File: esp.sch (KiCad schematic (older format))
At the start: 11 parts, among them J1 JTAG, U1 ESP32-WROOM-32

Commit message: Added images Added information to schematic Added information to layout
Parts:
- renumbered C5 to C4, C6 to C5
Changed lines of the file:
@@
 encoding utf-8
 Sheet 2 11
-Title ""
-Date ""
-Rev ""
-Comp ""
-Comment1 ""
+Title "AirMon"
+Date "2020-01-13"
+Rev "0.1"
+Comp "Jörg Bayer"
+Comment1 "CC BY 4.0"
 Comment2 ""
 Comment3 ""
@@
 U 1 1 5E199A3D
 P 4950 2900
-F 0 "D1" H 4942 2645 50  0000 C CNN
-F 1 "GREEN" H 4942 2736 50  0000 C CNN
+F 0 "D1" H 4900 3000 50  0000 C CNN
+F 1 "GREEN" H 5100 3000 50  0000 C CNN
 F 2 "Diode_SMD:D_0805_2012Metric" H 4950 2900 50  0001 C CNN
 F 3 "~" H 4950 2900 50  0001 C CNN
@@
 AR Path="/5DD6D4DA/5DDED074/5DEEC855" Ref="C?"  Part="1"
 AR Path="/5E15DEC3/5DEEC855" Ref="C?"  Part="1"
-AR Path="/5E151517/5DEEC855" Ref="C5"  Part="1"
-F 0 "C5" H 4915 4596 50  0000 L CNN
+AR Path="/5E151517/5DEEC855" Ref="C4"  Part="1"
+F 0 "C4" H 4915 4596 50  0000 L CNN
 F 1 "100n" H 4915 4505 50  0000 L CNN
 F 2 "Capacitor_SMD:C_0603_1608Metric" H 4838 4400 50  0001 C CNN
@@
 AR Path="/5DD6D4DA/5DDED074/5E1DF3B6" Ref="C?"  Part="1"
 AR Path="/5E15DEC3/5E1DF3B6" Ref="C?"  Part="1"
-AR Path="/5E151517/5E1DF3B6" Ref="C6"  Part="1"
-F 0 "C6" H 5715 2996 50  0000 L CNN
+AR Path="/5E151517/5E1DF3B6" Ref="C5"  Part="1"
+F 0 "C5" H 5715 2996 50  0000 L CNN
 F 1 "100n" H 5715 2905 50  0000 L CNN
 F 2 "Capacitor_SMD:C_0603_1608Metric" H 5638 2800 50  0001 C CNN

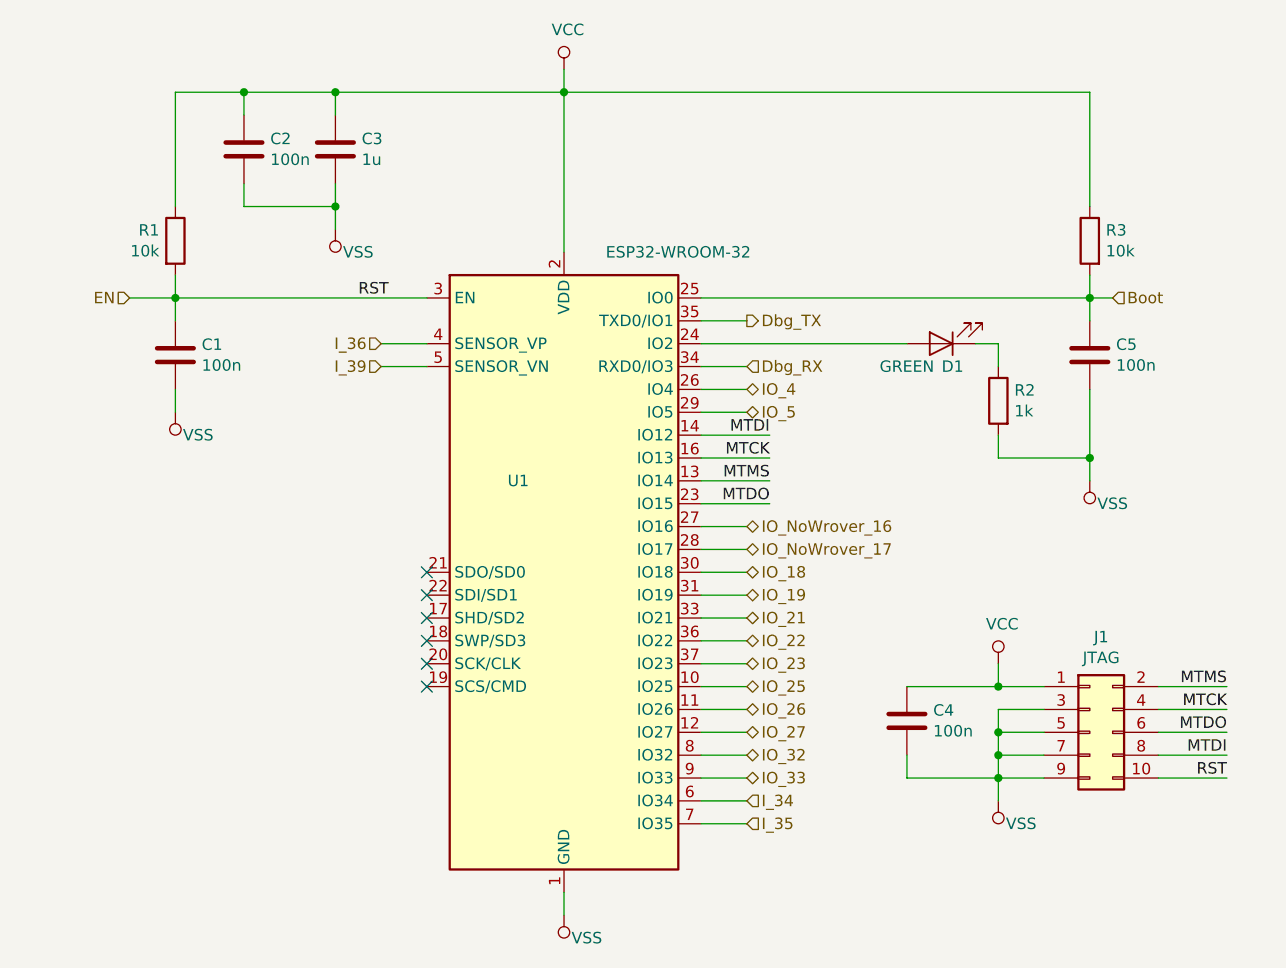
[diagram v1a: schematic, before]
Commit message: Added fuse for USB Added buttons for boot and reset Added version number to PCB Changed several component values for improved manufacturing Added BOM Added component position file
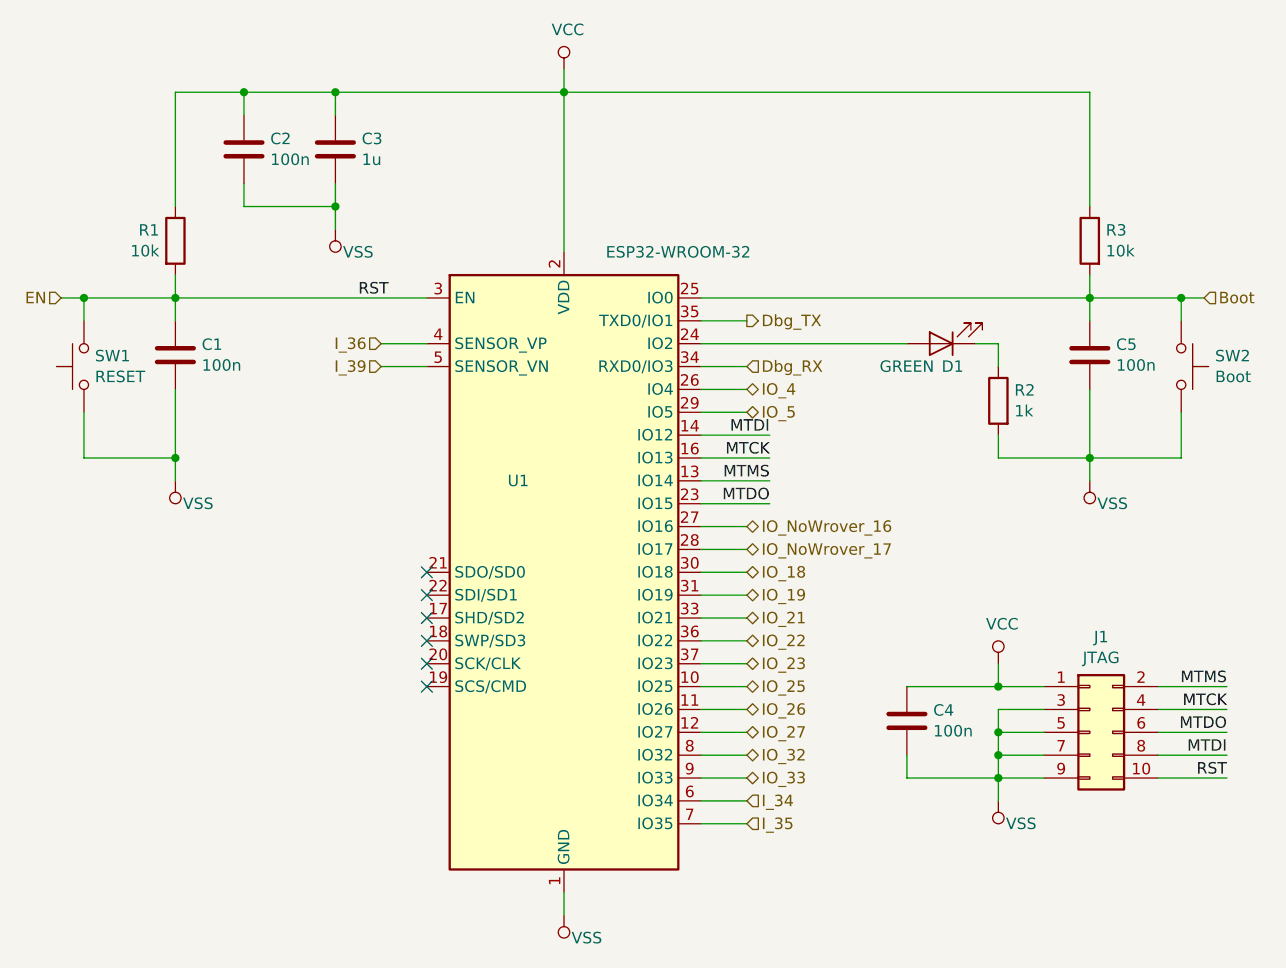
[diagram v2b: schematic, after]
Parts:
- added SW1: RESET, Button_Switch_SMD:SW_SPST_SKQG_WithStem, symbol Switch:SW_Push
- added SW2: Boot, Button_Switch_SMD:SW_SPST_SKQG_WithStem, symbol Switch:SW_Push
- C1, C2, C4, C5: lcsc# (none) -> C14663; manf# CL10B104KB8NNNL -> CC0603KRX7R9BB104
- C3: lcsc# (none) -> C28323; manf# CL21B105KBFNNNG -> CL21B105KBFNNNE
- D1: lcsc# (none) -> C2297
- J1: lcsc# (none) -> C180221; manf# (none) -> 20021221-00010C4LF
- R1, R3: lcsc# (none) -> C25804; manf# (none) -> 0603WAF1002T5E
- R2: lcsc# (none) -> C17513; manf# (none) -> 0805W8F1001T5E
- U1: manf# (none) -> ESP32-WROOM-32
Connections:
- net Boot: now also SW2.1
- net EN: now also SW1.1
- net VSS: now also SW1.2, SW2.2
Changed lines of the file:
@@
 F 2 "RF_Module:ESP32-WROOM-32" H 3300 2400 50  0001 C CNN
 F 3 "https://www.espressif.com/sites/default/files/documentation/esp32-wroom-32_datasheet_en.pdf" H 3000 3950 50  0001 C CNN
+F 4 "ESP32-WROOM-32" H 0   0   50  0001 C CNN "manf#"
 	1    3300 3900
 	1    0    0    -1
@@
 F 2 "Diode_SMD:D_0805_2012Metric" H 4950 2900 50  0001 C CNN
 F 3 "~" H 4950 2900 50  0001 C CNN
+F 4 "C2297" H 0   0   50  0001 C CNN "lcsc#"
 	1    4950 2900
 	-1   0    0    1
@@
 F 2 "Resistor_SMD:R_0805_2012Metric" V 5130 3150 50  0001 C CNN
 F 3 "~" H 5200 3150 50  0001 C CNN
+F 4 "C17513" H 0   0   50  0001 C CNN "lcsc#"
+F 5 "0805W8F1001T5E" H 0   0   50  0001 C CNN "manf#"
 	1    5200 3150
 	-1   0    0    -1
@@
 Wire Wire Line
 	5100 2900 5200 2900
-Text HLabel 1400 2700 0    50   Input ~ 0
+Text HLabel 1100 2700 0    50   Input ~ 0
 EN
 Wire Wire Line
@@
 F 2 "Resistor_SMD:R_0603_1608Metric" V 1530 2450 50  0001 C CNN
 F 3 "~" H 1600 2450 50  0001 C CNN
+F 4 "C25804" H 0   0   50  0001 C CNN "lcsc#"
+F 5 "0603WAF1002T5E" H 0   0   50  0001 C CNN "manf#"
 	1    1600 2450
 	1    0    0    -1
@@
 Wire Wire Line
 	1600 1800 1600 2300
-Text HLabel 5700 2700 2    50   Input ~ 0
+Text HLabel 6100 2700 2    50   Input ~ 0
 Boot
 Wire Wire Line
@@
 F 2 "Resistor_SMD:R_0603_1608Metric" V 5530 2450 50  0001 C CNN
 F 3 "~" H 5600 2450 50  0001 C CNN
+F 4 "C25804" H 0   0   50  0001 C CNN "lcsc#"
+F 5 "0603WAF1002T5E" H 0   0   50  0001 C CNN "manf#"
 	1    5600 2450
 	-1   0    0    -1
@@
 F 2 "Capacitor_SMD:C_0603_1608Metric" H 1938 1900 50  0001 C CNN
 F 3 "~" H 1900 2050 50  0001 C CNN
-F 4 "CL10B104KB8NNNL" H 1900 2050 50  0001 C CNN "manf#"
+F 4 "CC0603KRX7R9BB104" H 1900 2050 50  0001 C CNN "manf#"
+F 5 "C14663" H 0   0   50  0001 C CNN "lcsc#"
 	1    1900 2050
 	1    0    0    -1
@@
 F 2 "Capacitor_SMD:C_0805_2012Metric" H 2338 1900 50  0001 C CNN
 F 3 "~" H 2300 2050 50  0001 C CNN
-F 4 "CL21B105KBFNNNG" H 2300 2050 50  0001 C CNN "manf#"
+F 4 "CL21B105KBFNNNE" H 2300 2050 50  0001 C CNN "manf#"
+F 5 "C28323" H 0   0   50  0001 C CNN "lcsc#"
 	1    2300 2050
 	1    0    0    -1
@@
 F 2 "Connector_PinHeader_1.27mm:PinHeader_2x05_P1.27mm_Vertical_SMD" H 5600 4600 50  0001 C CNN
 F 3 "~" H 5600 4600 50  0001 C CNN
+F 4 "20021221-00010C4LF" H 5600 4600 50  0001 C CNN "manf#"
+F 5 "C180221" H 5600 4600 50  0001 C CNN "lcsc#"
 	1    5600 4600
 	1    0    0    -1
@@
 F 2 "Capacitor_SMD:C_0603_1608Metric" H 4838 4400 50  0001 C CNN
 F 3 "~" H 4800 4550 50  0001 C CNN
-F 4 "CL10B104KB8NNNL" H 4800 4550 50  0001 C CNN "manf#"
+F 4 "CC0603KRX7R9BB104" H 4800 4550 50  0001 C CNN "manf#"
+F 5 "C14663" H 0   0   50  0001 C CNN "lcsc#"
 	1    4800 4550
 	1    0    0    -1
@@
 L power:VSS #PWR?
 U 1 1 5E5E161C
-P 1600 3200
+P 1600 3500
 AR Path="/5DD6D4DA/5DEBB035/5E5E161C" Ref="#PWR?"  Part="1"
 AR Path="/5E15DEC3/5E5E161C" Ref="#PWR?"  Part="1"
 AR Path="/5E151517/5E5E161C" Ref="#PWR01"  Part="1"
-F 0 "#PWR01" H 1600 3050 50  0001 C CNN
-F 1 "VSS" H 1500 3300 50  0000 C CNN
-F 2 "" H 1600 3200 50  0001 C CNN
-F 3 "" H 1600 3200 50  0001 C CNN
-	1    1600 3200
+F 0 "#PWR01" H 1600 3350 50  0001 C CNN
+F 1 "VSS" H 1500 3600 50  0000 C CNN
+F 2 "" H 1600 3500 50  0001 C CNN
+F 3 "" H 1600 3500 50  0001 C CNN
+	1    1600 3500
 	-1   0    0    1
 $EndComp
@@
 	4100 4900 3900 4900
 Wire Wire Line
-	1400 2700 1600 2700
+	1100 2700 1200 2700
 $Comp
 L Device:C C?
@@
 F 2 "Capacitor_SMD:C_0603_1608Metric" H 1638 2800 50  0001 C CNN
 F 3 "~" H 1600 2950 50  0001 C CNN
-F 4 "CL10B104KB8NNNL" H 1600 2950 50  0001 C CNN "manf#"
+F 4 "CC0603KRX7R9BB104" H 1600 2950 50  0001 C CNN "manf#"
+F 5 "C14663" H 0   0   50  0001 C CNN "lcsc#"
 	1    1600 2950
 	1    0    0    -1
 $EndComp
 Wire Wire Line
-	1600 3100 1600 3200
+	1600 3100 1600 3400
 $Comp
 L Device:C C?
@@
 F 2 "Capacitor_SMD:C_0603_1608Metric" H 5638 2800 50  0001 C CNN
 F 3 "~" H 5600 2950 50  0001 C CNN
-F 4 "CL10B104KB8NNNL" H 5600 2950 50  0001 C CNN "manf#"
+F 4 "CC0603KRX7R9BB104" H 5600 2950 50  0001 C CNN "manf#"
+F 5 "C14663" H 0   0   50  0001 C CNN "lcsc#"
 	1    5600 2950
 	1    0    0    -1
@@
 Connection ~ 5600 3400
 Wire Wire Line
-	5600 2700 5700 2700
+	5600 2700 6000 2700
 Wire Wire Line
 	2300 1800 3300 1800
+$Comp
+L Switch:SW_Push SW2
+U 1 1 5E2178F1
+P 6000 3000
+F 0 "SW2" V 5954 3148 50  0000 L CNN
+F 1 "Boot" V 6045 3148 50  0000 L CNN
+F 2 "Button_Switch_SMD:SW_SPST_SKQG_WithStem" H 6000 3200 50  0001 C CNN
+F 3 "" H 6000 3200 50  0001 C CNN
+F 4 "C318889" H 0   0   50  0001 C CNN "lcsc#"
+F 5 "TS-1187A-C-C-B" H 0   0   50  0001 C CNN "manf#"
+	1    6000 3000
+	0    1    1    0
+$EndComp
+Wire Wire Line
+	6000 2800 6000 2700
+Connection ~ 6000 2700
+Wire Wire Line
+	6000 2700 6100 2700
+Wire Wire Line
+	5600 3400 6000 3400
+Wire Wire Line
+	6000 3400 6000 3200
+$Comp
+L Switch:SW_Push SW1
+U 1 1 5E225C7B
+P 1200 3000
+F 0 "SW1" V 1154 2952 50  0000 R CNN
+F 1 "RESET" V 1245 2952 50  0000 R CNN
+F 2 "Button_Switch_SMD:SW_SPST_SKQG_WithStem" H 1200 3200 50  0001 C CNN
+F 3 "" H 1200 3200 50  0001 C CNN
+F 4 "C318889" H 0   0   50  0001 C CNN "lcsc#"
+F 5 "TS-1187A-C-C-B" H 0   0   50  0001 C CNN "manf#"
+	1    1200 3000
+	0    -1   1    0
+$EndComp
+Wire Wire Line
+	1200 2800 1200 2700
+Connection ~ 1200 2700
+Wire Wire Line
+	1200 2700 1600 2700
+Wire Wire Line
+	1200 3200 1200 3400
+Wire Wire Line
+	1200 3400 1600 3400
+Connection ~ 1600 3400
+Wire Wire Line
+	1600 3400 1600 3500
 $EndSCHEMATC
